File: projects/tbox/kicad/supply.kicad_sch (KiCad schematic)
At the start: 32 parts, among them J2501 PWR IN (panel Powerpole), U2501 ADP7142AUJZ-5.0, U2502 OPA1678, U2503 TPS7A4701

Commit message: Review fixes, mechanical: footprints, switch codes, PTC and LED resistors
- TY-250P footprint: stray ')' truncated the body/courtyard/silk; fixed
  (transformers now have a courtyard on the board).
- SJ-43514: tip pad at +3.6 from the axis, pin-5 hole at +1.6 (3.2 from
  pin 3) per a closer reading of the SJ-4351X drawing.
- C&K 7101 AV2 and 7201/7203 V-bracket: terminal holes 1.85 mm (0.073 in)
  per catalog pages F-11/F-13; DPDT terminal columns 0.190 in apart and
  bracket legs 0.250 in apart (they were swapped).
- Switch functions: PVA OA is momentary and EE is push-push, so PTT/
  intercom get OA and the mutes EE; override toggle 7201 (on-none-on)
  -> 7203 (on-off-on).
- PTC MPN 1812L050/60MR; TX LED resistor 680R -> 2k2 and all seven LED
  resistors to 0805.
Board footprints refreshed in place; the resulting courtyard overlaps are
resolved by the placement fixes that follow.
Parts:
- F2501: MPN 1812L050/60DR -> 1812L050/60MR
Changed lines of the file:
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@@
 			)
 		)
-		(property "MPN" "1812L050/60DR"
+		(property "MPN" "1812L050/60MR"
 			(at 38.1 50.8 0)
 			(hide yes)

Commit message: Review fixes, tooling: parts stay on their board, panel datums, V-cut keepouts, regulator caps, stricter checkers
- place_panel: rear board is 180..270 (was 250); cluster and refinement
  placement can no longer cross a V-score; top-panel parts are placed by
  their shaft/plunger datum (DATUM table), not the footprint origin.
- New tools/check_placement.py: every footprint inside its board's band
  (jack noses may overhang the outer edges) and no non-power net spans
  boards without a ribbon connector. Board re-placed: 0 problems, no
  courtyard overlaps.
- setup_pcb: copper keepout rule areas +-1 mm about each V-score on all
  four copper layers (tracks, vias, pads, fills).
- place_decoupling: band by the cap's own board; targets are power pins
  only (SENSE/EN excluded, from the netlist); converters get the bulk caps
  on their rails first -- C2513 is now at the TPS7A4701 OUT pin.
- power_model/check_power: Load_mA must parse as finite, non-negative,
  typ<=max; any part with a power_in pin on a rail must carry one; an
  empty netlist or any model warning fails the check. The five
  TS12A12511s get Load_mA 0/0.01.
- gen_power_tree: strip_managed walks parens string-aware.
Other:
- note added: "load: 62 typ / 250.1 max mA (direct 62/248.1 + downstream)"
- note removed: "load: 62 typ / 250 max mA (direct 62/248 + downstream)"
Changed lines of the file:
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@@
 		)
 	)
-	(text "electret bias"
-		(exclude_from_sim no)
-		(at 91.44 80.01 0)
-		(effects
-			(font
-				(size 1.27 1.27)
-			)
-			(justify left bottom)
-		)
-	)
 	(text "U2503 TPS7A4701 (ANY-OUT): 1.4 + 6.4 + 0.8 + 0.4 = 9.0 V -- pins 5/9/10 to GND, other set pins open. SENSE to OUT, EN to IN."
 		(exclude_from_sim no)
@@
 		)
 	)
-	(text "DC bias only, no load by design"
-		(exclude_from_sim no)
-		(at 73.66 125.73 0)
-		(effects
-			(font
-				(size 1.27 1.27)
-			)
-			(justify left bottom)
-		)
-	)
-	(text "Pd <=1.5W @15V; dropout OK to 10V5"
-		(exclude_from_sim no)
-		(at 213.36 73.66 0)
-		(effects
-			(font
-				(size 1.27 1.27)
-			)
-			(justify left bottom)
-		)
-	)
-	(text "load: 0 typ / 2 max mA"
-		(exclude_from_sim no)
-		(at 91.44 77.47 0)
-		(effects
-			(font
-				(size 1.27 1.27)
-			)
-			(justify left bottom)
-		)
-	)
-	(text "load: 62 typ / 250 max mA (direct 62/248 + downstream)"
-		(exclude_from_sim no)
-		(at 213.36 71.12 0)
-		(effects
-			(font
-				(size 1.27 1.27)
-			)
-			(justify left bottom)
-		)
-	)
 	(junction
 		(at 55.88 78.74)
@@
 		(color 0 0 0 0)
 	)
+  (text "Pd <=1.5W @15V; dropout OK to 10V5" (exclude_from_sim no) (at 213.36 73.66 0) (effects (font (size 1.27 1.27)) (justify left bottom)))
+  (text "load: 62 typ / 250.1 max mA (direct 62/248.1 + downstream)" (exclude_from_sim no) (at 213.36 71.12 0) (effects (font (size 1.27 1.27)) (justify left bottom)))
+  (text "electret bias" (exclude_from_sim no) (at 91.44 80.01 0) (effects (font (size 1.27 1.27)) (justify left bottom)))
+  (text "load: 0 typ / 2 max mA" (exclude_from_sim no) (at 91.44 77.47 0) (effects (font (size 1.27 1.27)) (justify left bottom)))
+  (text "DC bias only, no load by design" (exclude_from_sim no) (at 73.66 125.73 0) (effects (font (size 1.27 1.27)) (justify left bottom)))
 )

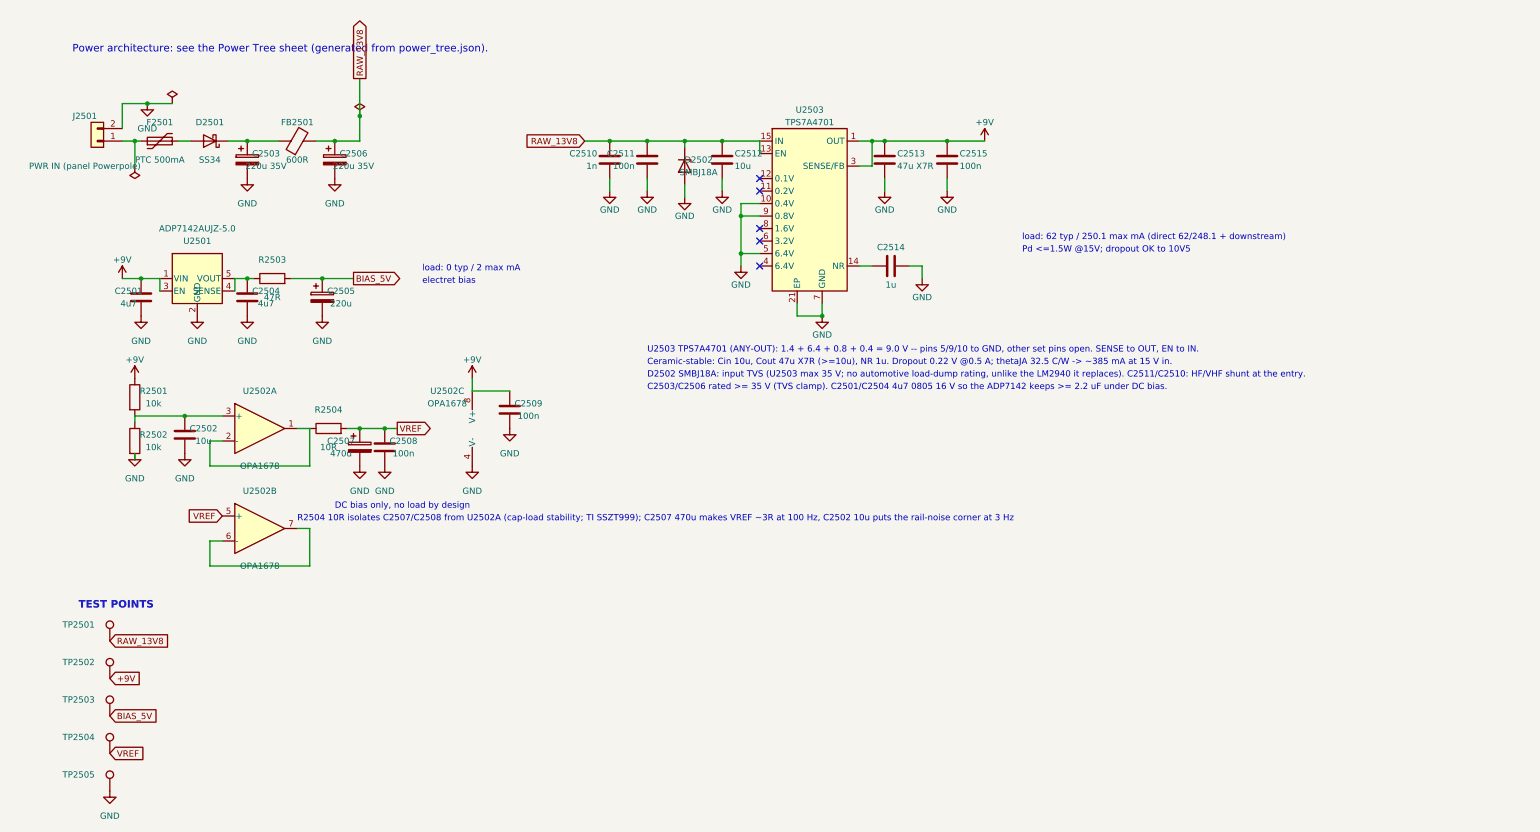
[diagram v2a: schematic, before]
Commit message: Review design changes: chassis returns, OPA1622 phones amps, RX-in protection, supervisor, mute fade, gains, BLEND buffer, jack-side protection, mic-jack bias
Decisions Q1-Q9 from the 2026-09-08 adversarial review:
- Q1 (D): phones jack sleeves and TRRS ring 2 on CHASSIS; GND-CHASSIS
  ties per board (NT1001 front at the headset jacks, NT2401 control at
  the phones amps, NT3201 rear) with chassis studs H1001/H2401; phones
  return rides the chassis, never the ribbon ground.
- Q2 (B'): U2401/U2403 NJM4556A -> OPA1622 (new tbox symbol, VSON-10),
  build-out 10R -> 3R3, EN from PWR_OK.
- Q3 (A+C): RX-in coupling caps non-polar 10u, 2k2 series, 1N4148W
  clamps to the rails at the op-amp inputs (SMAJ15CA stays at the jack).
- Q4 (B): TPS3808G01 supervisor on +9 V (7.5 V, ~1.2 s) -> PWR_OK;
  MUTE_HOLD inverter replaces the RC hold, shunts PTT_ACTIVE; Q3201 gets
  a 100k gate pull-down.
- Q5 (A): mute fades (2k2 + back-to-back 2N7002 shunt to Vref, ~5 ms)
  before the TS12A12511 switches (~30 ms, immediate release).
- Q6 (A): preamp LO +28 / HI +40 dB (R1104 430R, R1106 3k3).
- Q7 (A): BLEND is an inverting summer on U3301B (R3318 22k, C3317).
- Q8 (C): phones RF filters move to the front board at the jacks; SP724
  arrays on every front jack contact and the rear PTT inputs; SMAJ15CA
  across each isolated line-out secondary.
- Q9 (B'): 3.5 mm mic jack tip carries the mic, tip and ring both get
  2k2 bias (R1109/C1109).
DESIGN.md, LEVELS.md and TODO.md updated; ERC 0, check_sch/boards/
footprints/power clean; power tree regenerated.
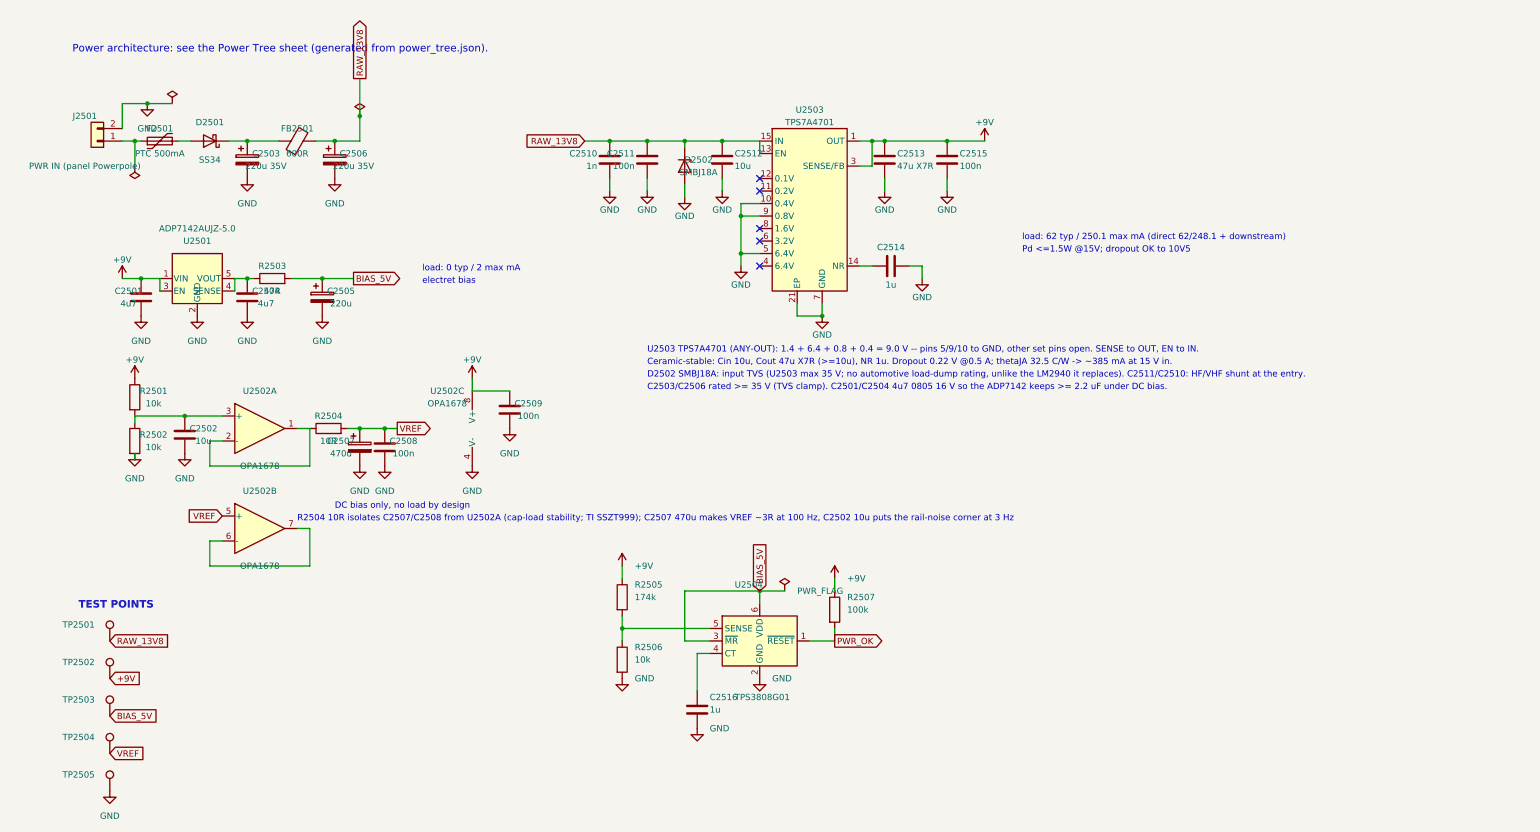
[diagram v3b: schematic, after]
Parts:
- added C2516: 1u, Capacitor_SMD:C_0603_1608Metric, symbol Device:C
- added R2505: 174k, Resistor_SMD:R_0603_1608Metric, symbol Device:R
- added R2506: 10k, Resistor_SMD:R_0603_1608Metric, symbol Device:R
- added R2507: 100k, Resistor_SMD:R_0603_1608Metric, symbol Device:R
- added U2504: TPS3808G01, Package_TO_SOT_SMD:SOT-23-6, symbol Power_Supervisor:TPS3808DBV
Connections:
- net +9V: now also R2505.1, R2507.1
- net BIAS_5V: now also U2504.3 (~{MR}), U2504.6 (VDD)
- net GND: now also C2516.2, R2506.2, U2504.2 (GND)
- new net: C2516.1, U2504.4 (CT)
- new net: R2505.2, R2506.1, U2504.5 (SENSE)
- new net PWR_OK: R2507.2, U2504.1 (~{RESET})

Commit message: Review 2 fixes: PWR_OK pull-up and supervisor bypass on the 5 V rail, CT 220n, ring-bias load, ribbon reach check, doc contradictions
- TPS3808 RESET is rated 6.5 V (7 V abs max): R2507 now pulls PWR_OK up to
  BIAS_5V, which is also VDD; C2517 100n bypasses VDD at the part.
- C2516 220n: tD = CT(nF)/175 + 0.5 ms, so 1u was 5.7 s, not 1.2 s.
- R1109/R1309 ring-bias resistors carry Load_mA 0/1 on BIAS_5V.
- C2513 47u X7R 25V, MPN GRM32ER71E476KE15L.
- check_placement: a net that spans boards must reach every one of them
  through a cable present at both ends, not just touch any ribbon.
- DESIGN.md: Vref is the mute/summing reference, not DC bias only; three
  chassis ties, not NT3201 alone; supervisor text matches the schematic.
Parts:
- added C2517: 100n, Capacitor_SMD:C_0603_1608Metric, symbol Device:C
- C2513: value 47u X7R -> 47u X7R 25V; MPN (none) -> GRM32ER71E476KE15L
- C2516: value 1u -> 220n
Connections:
- net +9V: no longer R2507.1
- net BIAS_5V: now also R2507.1, C2517.1
- net GND: now also C2517.2
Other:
- note added: "load: 0.02 typ / 4.02 max mA"
- note added: "load: 54.02 typ / 262.1 max mA (direct 54/258.1 + downstream)"
- note removed: "load: 0 typ / 2 max mA"
- note removed: "load: 62 typ / 250.1 max mA (direct 62/248.1 + downstream)"
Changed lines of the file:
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@@
 			)
 		)
-		(property "Value" "47u X7R"
+		(property "Value" "47u X7R 25V"
 			(at 187.96 55.88 0)
 			(show_name no)
@@
 			)
 		)
+		(property "MPN" "GRM32ER71E476KE15L"
+			(at 185.42 54.61 0)
+			(show_name no)
+			(do_not_autoplace no)
+			(hide yes)
+			(effects
+				(font
+					(size 1.27 1.27)
+				)
+			)
+		)
 		(property "Footprint" "Capacitor_SMD:C_1210_3225Metric"
 			(at 185.42 54.61 0)
@@
 		(color 0 0 0 0)
 	)
-  (text "Pd <=1.5W @15V; dropout OK to 10V5" (exclude_from_sim no) (at 213.36 73.66 0) (effects (font (size 1.27 1.27)) (justify left bottom)))
-  (text "load: 62 typ / 250.1 max mA (direct 62/248.1 + downstream)" (exclude_from_sim no) (at 213.36 71.12 0) (effects (font (size 1.27 1.27)) (justify left bottom)))
-  (text "electret bias" (exclude_from_sim no) (at 91.44 80.01 0) (effects (font (size 1.27 1.27)) (justify left bottom)))
-  (text "load: 0 typ / 2 max mA" (exclude_from_sim no) (at 91.44 77.47 0) (effects (font (size 1.27 1.27)) (justify left bottom)))
-  (text "DC bias only, no load by design" (exclude_from_sim no) (at 73.66 125.73 0) (effects (font (size 1.27 1.27)) (justify left bottom)))
 	(symbol
 		(lib_id "Power_Supervisor:TPS3808DBV")
@@
 			)
 		)
-		(property "Value" "1u"
+		(property "Value" "220n"
 			(at 149.86 166.37 0)
 			(show_name no)
@@
 	(wire
 		(pts
-			(xy 175.26 142.24) (xy 175.26 139.7)
+			(xy 160.02 142.24) (xy 165.1 142.24)
 		)
 		(stroke
@@
 		)
 	)
+	(junction
+		(at 160.02 142.24)
+		(diameter 0)
+		(color 0 0 0 0)
+	)
 	(symbol
-		(lib_id "power:+9V")
-		(at 175.26 139.7 0)
+		(lib_id "power:PWR_FLAG")
+		(at 165.1 142.24 0)
 		(unit 1)
 		(exclude_from_sim no)
@@
 		(on_board yes)
 		(dnp no)
-		(property "Reference" "#PWR02532"
-			(at 177.8 137.16 0)
+		(property "Reference" "#FLG02504"
+			(at 167.64 139.7 0)
 			(show_name no)
 			(do_not_autoplace no)
@@
 			)
 		)
-		(property "Value" "+9V"
-			(at 177.8 139.7 0)
+		(property "Value" "PWR_FLAG"
+			(at 167.64 142.24 0)
 			(show_name no)
 			(do_not_autoplace no)
@@
 		)
 		(property "Footprint" ""
-			(at 175.26 139.7 0)
+			(at 165.1 142.24 0)
 			(show_name no)
 			(do_not_autoplace no)
@@
 		)
 		(property "Datasheet" ""
-			(at 175.26 139.7 0)
+			(at 165.1 142.24 0)
 			(show_name no)
 			(do_not_autoplace no)
@@
 		)
 		(property "Description" ""
-			(at 175.26 139.7 0)
+			(at 165.1 142.24 0)
 			(show_name no)
 			(do_not_autoplace no)
@@
 			(project "tbox"
 				(path "/6a29b3f1-3e67-482d-942d-4557fa8bc2d6/7885f5d1-bf3d-5361-a0a2-98a329efbaa8/ec376872-0fd3-415b-977e-2d7984375c54"
-					(reference "#PWR02532")
+					(reference "#FLG02504")
 					(unit 1)
 				)
@@
 	(wire
 		(pts
-			(xy 160.02 142.24) (xy 165.1 142.24)
+			(xy 165.1 142.24) (xy 175.26 142.24)
 		)
 		(stroke
@@
 	)
 	(junction
-		(at 160.02 142.24)
+		(at 165.1 142.24)
+		(diameter 0)
+		(color 0 0 0 0)
+	)
+	(wire
+		(pts
+			(xy 175.26 142.24) (xy 187.96 142.24)
+		)
+		(stroke
+			(width 0)
+			(type default)
+		)
+	)
+	(junction
+		(at 175.26 142.24)
 		(diameter 0)
 		(color 0 0 0 0)
 	)
 	(symbol
-		(lib_id "power:PWR_FLAG")
-		(at 165.1 142.24 0)
+		(lib_id "Device:C")
+		(at 187.96 146.05 0)
 		(unit 1)
 		(exclude_from_sim no)
@@
 		(on_board yes)
 		(dnp no)
-		(property "Reference" "#FLG02504"
-			(at 167.64 139.7 0)
+		(property "Reference" "C2517"
+			(at 190.5 143.51 0)
+			(show_name no)
+			(do_not_autoplace no)
+			(effects
+				(font
+					(size 1.27 1.27)
+				)
+				(justify left)
+			)
+		)
+		(property "Value" "100n"
+			(at 190.5 146.05 0)
+			(show_name no)
+			(do_not_autoplace no)
+			(effects
+				(font
+					(size 1.27 1.27)
+				)
+				(justify left)
+			)
+		)
+		(property "Footprint" "Capacitor_SMD:C_0603_1608Metric"
+			(at 187.96 146.05 0)
 			(show_name no)
 			(do_not_autoplace no)
@@
 			)
 		)
-		(property "Value" "PWR_FLAG"
-			(at 167.64 142.24 0)
+		(property "Datasheet" ""
+			(at 187.96 146.05 0)
+			(show_name no)
+			(do_not_autoplace no)
+			(hide yes)
+			(effects
+				(font
+					(size 1.27 1.27)
+				)
+				(justify left)
+			)
+		)
+		(property "Description" ""
+			(at 187.96 146.05 0)
+			(show_name no)
+			(do_not_autoplace no)
+			(hide yes)
+			(effects
+				(font
+					(size 1.27 1.27)
+				)
+				(justify left)
+			)
+		)
+		(pin "1"
+		)
+		(pin "2"
+		)
+		(instances
+			(project "tbox"
+				(path "/6a29b3f1-3e67-482d-942d-4557fa8bc2d6/7885f5d1-bf3d-5361-a0a2-98a329efbaa8/ec376872-0fd3-415b-977e-2d7984375c54"
+					(reference "C2517")
+					(unit 1)
+				)
+			)
+		)
+	)
+	(symbol
+		(lib_id "power:GND")
+		(at 187.96 149.86 0)
+		(unit 1)
+		(exclude_from_sim no)
+		(in_bom yes)
+		(on_board yes)
+		(dnp no)
+		(property "Reference" "#PWR02532"
+			(at 190.5 147.32 0)
+			(show_name no)
+			(do_not_autoplace no)
+			(hide yes)
+			(effects
+				(font
+					(size 1.27 1.27)
+				)
+				(justify left)
+			)
+		)
+		(property "Value" "GND"
+			(at 190.5 149.86 0)
 			(show_name no)
 			(do_not_autoplace no)
@@
 		)
 		(property "Footprint" ""
-			(at 165.1 142.24 0)
+			(at 187.96 149.86 0)
 			(show_name no)
 			(do_not_autoplace no)
@@
 		)
 		(property "Datasheet" ""
-			(at 165.1 142.24 0)
+			(at 187.96 149.86 0)
 			(show_name no)
 			(do_not_autoplace no)
@@
 		)
 		(property "Description" ""
-			(at 165.1 142.24 0)
+			(at 187.96 149.86 0)
 			(show_name no)
 			(do_not_autoplace no)
@@
 			(project "tbox"
 				(path "/6a29b3f1-3e67-482d-942d-4557fa8bc2d6/7885f5d1-bf3d-5361-a0a2-98a329efbaa8/ec376872-0fd3-415b-977e-2d7984375c54"
-					(reference "#FLG02504")
+					(reference "#PWR02532")
 					(unit 1)
 				)
@@
 		)
 	)
+  (text "Pd <=1.5W @15V; dropout OK to 10V5" (exclude_from_sim no) (at 213.36 73.66 0) (effects (font (size 1.27 1.27)) (justify left bottom)))
+  (text "load: 54.02 typ / 262.1 max mA (direct 54/258.1 + downstream)" (exclude_from_sim no) (at 213.36 71.12 0) (effects (font (size 1.27 1.27)) (justify left bottom)))
+  (text "electret bias" (exclude_from_sim no) (at 91.44 80.01 0) (effects (font (size 1.27 1.27)) (justify left bottom)))
+  (text "load: 0.02 typ / 4.02 max mA" (exclude_from_sim no) (at 91.44 77.47 0) (effects (font (size 1.27 1.27)) (justify left bottom)))
+  (text "DC bias only, no load by design" (exclude_from_sim no) (at 73.66 125.73 0) (effects (font (size 1.27 1.27)) (justify left bottom)))
 )

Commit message: Review 2: load maxima and the resistor rule
- Op-amp maxima from the datasheets: OPA1678 duals 4/6 (5.6 mA IQ over
  temperature), line drivers 4/10, OPA1622 6/101 (8.4 mA IQ + two
  145 mA-peak class-B channels).
- Every resistor with an end on a rail now needs Load_mA (Vref returns
  and the ADP7142 output RC exempt): R2122, R2501, R2505, R2507,
  R3209/R3210 (1k gain-select pull-ups, 9 mA each when closed),
  R3201/R3202 PTT pull-ups annotated.
- Load_mA syntax is strict (n or n/m).
- RAW_13V8 capability 400 mA (1812L050 hold at 50 C), not 500.
- C3401/C3402 10u X7R 25V, GRM31CR71E106KA12L.
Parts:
- R2501: Load_mA (none) -> 0.45
- R2505: Load_mA (none) -> 0.05
- R2507: Load_mA (none) -> 0/0.05
- U2502: Load_mA 4/5 -> 4/6
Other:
- note added: "load: 0.02 typ / 4.1 max mA"
- note added: "load: 54.6 typ / 306.6 max mA (direct 54.6/302.5 + downstream)"
- note removed: "load: 0.02 typ / 4.02 max mA"
- note removed: "load: 54.02 typ / 262.1 max mA (direct 54/258.1 + downstream)"
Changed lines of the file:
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@@
 			)
 		)
+		(property "Load_mA" "0.45"
+			(at 33.02 102.87 0)
+			(show_name no)
+			(do_not_autoplace no)
+			(hide yes)
+			(effects
+				(font
+					(size 1.27 1.27)
+				)
+			)
+		)
 		(property "Footprint" "Resistor_SMD:R_0603_1608Metric"
 			(at 33.02 102.87 0)
@@
 			)
 		)
-		(property "Load_mA" "4/5"
+		(property "Load_mA" "4/6"
 			(at 58.42 109.22 0)
 			(hide yes)
@@
 			)
 		)
+		(property "Load_mA" "0.05"
+			(at 132.08 143.51 0)
+			(show_name no)
+			(do_not_autoplace no)
+			(hide yes)
+			(effects
+				(font
+					(size 1.27 1.27)
+				)
+			)
+		)
 		(property "Footprint" "Resistor_SMD:R_0603_1608Metric"
 			(at 132.08 143.51 0)
@@
 			)
 		)
+		(property "Load_mA" "0/0.05"
+			(at 175.26 146.05 0)
+			(show_name no)
+			(do_not_autoplace no)
+			(hide yes)
+			(effects
+				(font
+					(size 1.27 1.27)
+				)
+			)
+		)
 		(property "Footprint" "Resistor_SMD:R_0603_1608Metric"
 			(at 175.26 146.05 0)
@@
 	)
   (text "Pd <=1.5W @15V; dropout OK to 10V5" (exclude_from_sim no) (at 213.36 73.66 0) (effects (font (size 1.27 1.27)) (justify left bottom)))
-  (text "load: 54.02 typ / 262.1 max mA (direct 54/258.1 + downstream)" (exclude_from_sim no) (at 213.36 71.12 0) (effects (font (size 1.27 1.27)) (justify left bottom)))
+  (text "load: 54.6 typ / 306.6 max mA (direct 54.6/302.5 + downstream)" (exclude_from_sim no) (at 213.36 71.12 0) (effects (font (size 1.27 1.27)) (justify left bottom)))
   (text "electret bias" (exclude_from_sim no) (at 91.44 80.01 0) (effects (font (size 1.27 1.27)) (justify left bottom)))
-  (text "load: 0.02 typ / 4.02 max mA" (exclude_from_sim no) (at 91.44 77.47 0) (effects (font (size 1.27 1.27)) (justify left bottom)))
+  (text "load: 0.02 typ / 4.1 max mA" (exclude_from_sim no) (at 91.44 77.47 0) (effects (font (size 1.27 1.27)) (justify left bottom)))
   (text "DC bias only, no load by design" (exclude_from_sim no) (at 73.66 125.73 0) (effects (font (size 1.27 1.27)) (justify left bottom)))
 )
